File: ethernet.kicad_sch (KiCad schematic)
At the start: 32 parts, among them J8 RJ45_Wuerth_74980111211, U3 KSZ8001L-TR, U4 SRV05-4

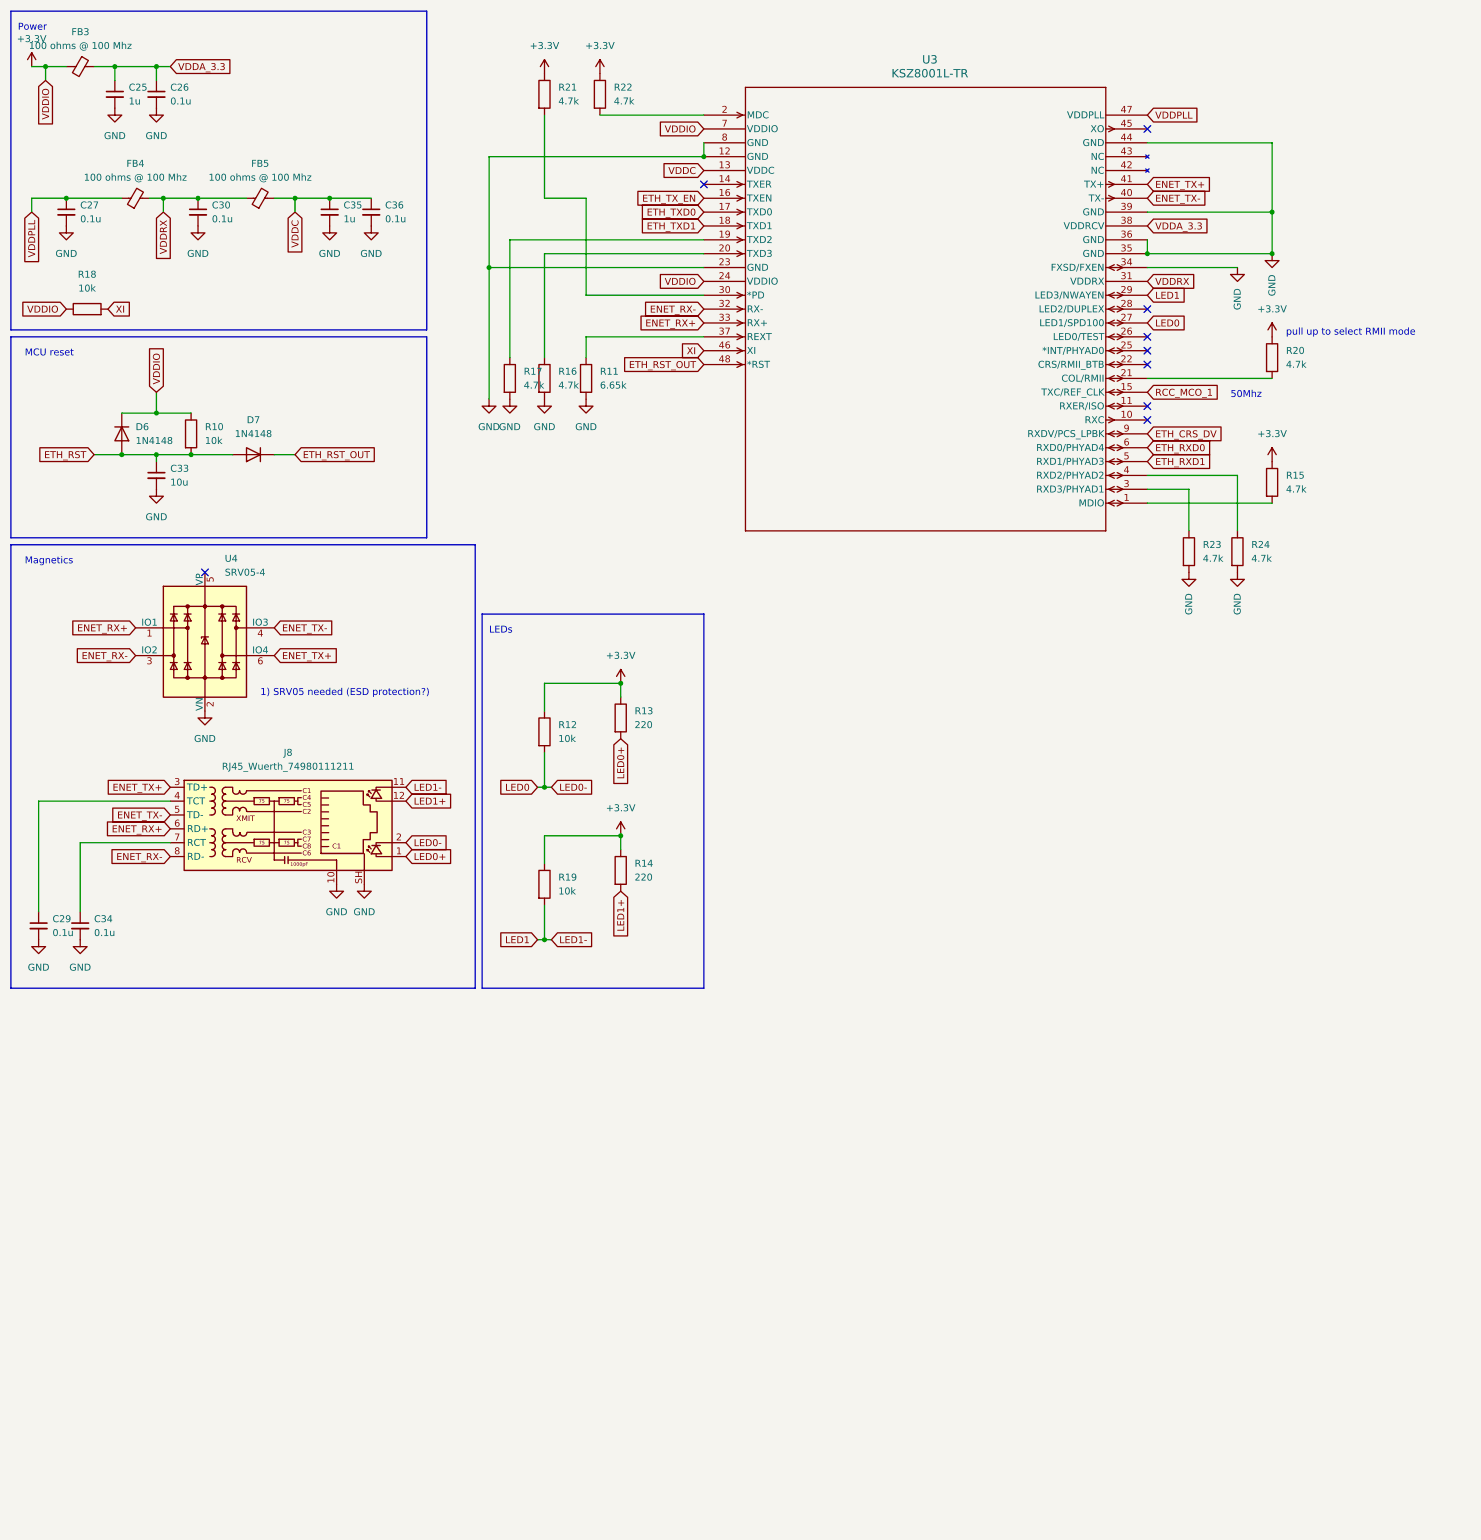
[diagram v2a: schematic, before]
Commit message: Switch over to using LAN8720A
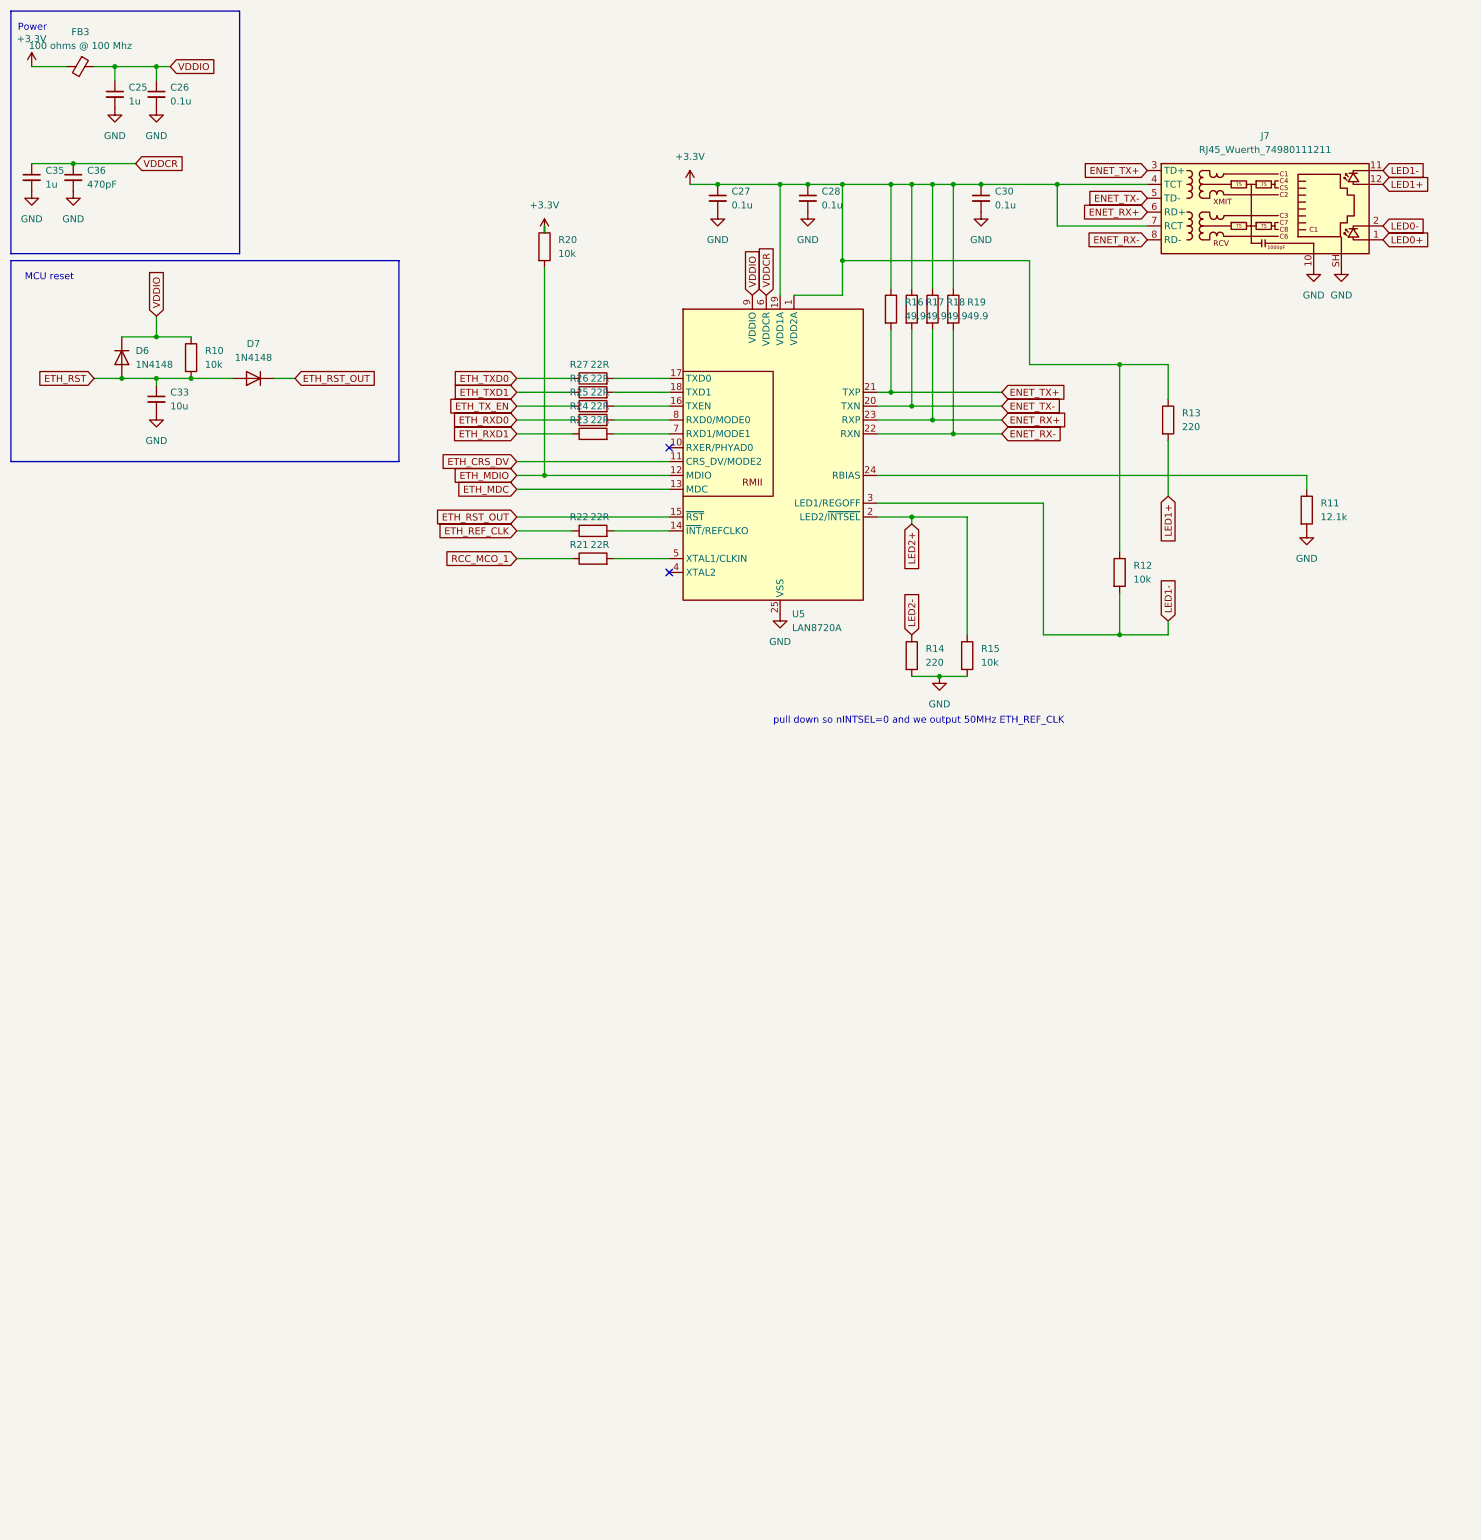
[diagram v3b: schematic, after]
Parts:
- removed C29, C34: 0.1u, symbol Device:C_Small
- removed FB4, FB5: 100 ohms @ 100 Mhz, symbol Device:FerriteBead_Small
- removed J8: RJ45_Wuerth_74980111211, Connector_RJ:RJ45_Wuerth_74980111211_Horizontal, symbol Connector:RJ45_Wuerth_74980111211
- removed U3: KSZ8001L-TR, LQFP-48_MCH, symbol 2024-02-18_02-27-55:KSZ8001L-TR
- removed U4: SRV05-4, Package_TO_SOT_SMD:SOT-23-6, symbol Power_Protection:SRV05-4
- added C28: 0.1u, symbol Device:C_Small
- added J7: RJ45_Wuerth_74980111211, Connector_RJ:RJ45_Wuerth_74980111211_Horizontal, symbol Connector:RJ45_Wuerth_74980111211
- added R25, R26, R27: 22R, symbol Device:R
- added U5: LAN8720A, Package_DFN_QFN:VQFN-24-1EP_4x4mm_P0.5mm_EP2.5x2.5mm_ThermalVias, symbol Interface_Ethernet:LAN8720A
- C36: value 0.1u -> 470pF
- R11: value 6.65k -> 12.1k
- R15, R20: value 4.7k -> 10k
- R16, R17: value 4.7k -> 49.9
- R18, R19: value 10k -> 49.9
- R21, R22, R23, R24: value 4.7k -> 22R
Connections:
- net LED1 is gone; now on net ENET_RX-: R19.2
- net VDDPLL is gone; now on net +3.3V: C27.1
- net VDDRX is gone; now on net +3.3V: C30.1
- net XI is gone; now on net ENET_RX+: R18.2
- net +3.3V: now also R16.1, R17.1, C28.1, J7.4 (TCT), J7.7 (RCT), U5.1 (VDD2A), U5.19 (VDD1A); no longer D6.1 (K), R10.1, R14.1, R15.1, R21.1, R22.1
- net ENET_RX+: now also J7.6 (RD+), U5.23 (RXP)
- net ENET_RX-: now also J7.8 (RD-), U5.22 (RXN)
- net ENET_TX+: now also R16.2, J7.3 (TD+), U5.21 (TXP)
- net ENET_TX-: now also R17.2, J7.5 (TD-), U5.20 (TXN)
- net ETH_CRS_DV: now also U5.11 (CRS_DV/MODE2)
- net ETH_RST_OUT: now also U5.15 (~{RST})
- net ETH_RXD0: now also R24.1
- net ETH_RXD1: now also R23.1
- net ETH_TXD0: now also R27.1
- net ETH_TXD1: now also R26.1
- net ETH_TX_EN: now also R25.1
- net GND: now also R14.2, R15.2, C28.2, J7.10, J7.SH, U5.25 (VSS); no longer R16.2, R17.2, R23.2, R24.2
- net LED0+: now also J7.1; no longer R13.2
- net LED1+: now also R13.2, J7.12; no longer R14.2
- net RCC_MCO_1: now also R21.1
- net at R11.1: now also U5.24 (RBIAS)
- net at R22.2: now also U5.14 (~{INT}/REFCLKO)
- net at R21.2: now also U5.5 (XTAL1/CLKIN)
- net ETH_MDIO: now reaches R20.2
- net ETH_MDIO: now also U5.12 (MDIO)
- net LED0 renamed LED1-
- net LED1-: now also J7.11, U5.3 (LED1/REGOFF)
- net VDDA_3.3 renamed VDDIO
- net VDDIO: now also D6.1 (K), R10.1, U5.9 (VDDIO)
- net VDDC renamed VDDCR
- net VDDCR: now also U5.6 (VDDCR)
- new net: R24.2, U5.8 (RXD0/MODE0)
- new net: R26.2, U5.18 (TXD1)
- new net: R27.2, U5.17 (TXD0)
- new net: R25.2, U5.16 (TXEN)
- new net: R23.2, U5.7 (RXD1/MODE1)
- new net ETH_MDC: U5.13 (MDC)
- new net ETH_REF_CLK: R22.1
- new net LED0-: J7.2
- new net LED2+: R15.1, U5.2 (LED2/~{INTSEL})
- new net LED2-: R14.1
- no-connect marks 9 -> 2
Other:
- note added: "pull down so nINTSEL=0 and we output 50MHz ETH_REF_CLK"
- note removed: "1) SRV05 needed (ESD protection?)"
- note removed: "50Mhz"
- note removed: "LEDs"
- note removed: "Magnetics"
- note removed: "pull up to select RMII mode"
- moved on the sheet: C33, C35, C36, D6, D7, R10, R12, R13

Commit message: Add USB circuit (peripheral mode only)
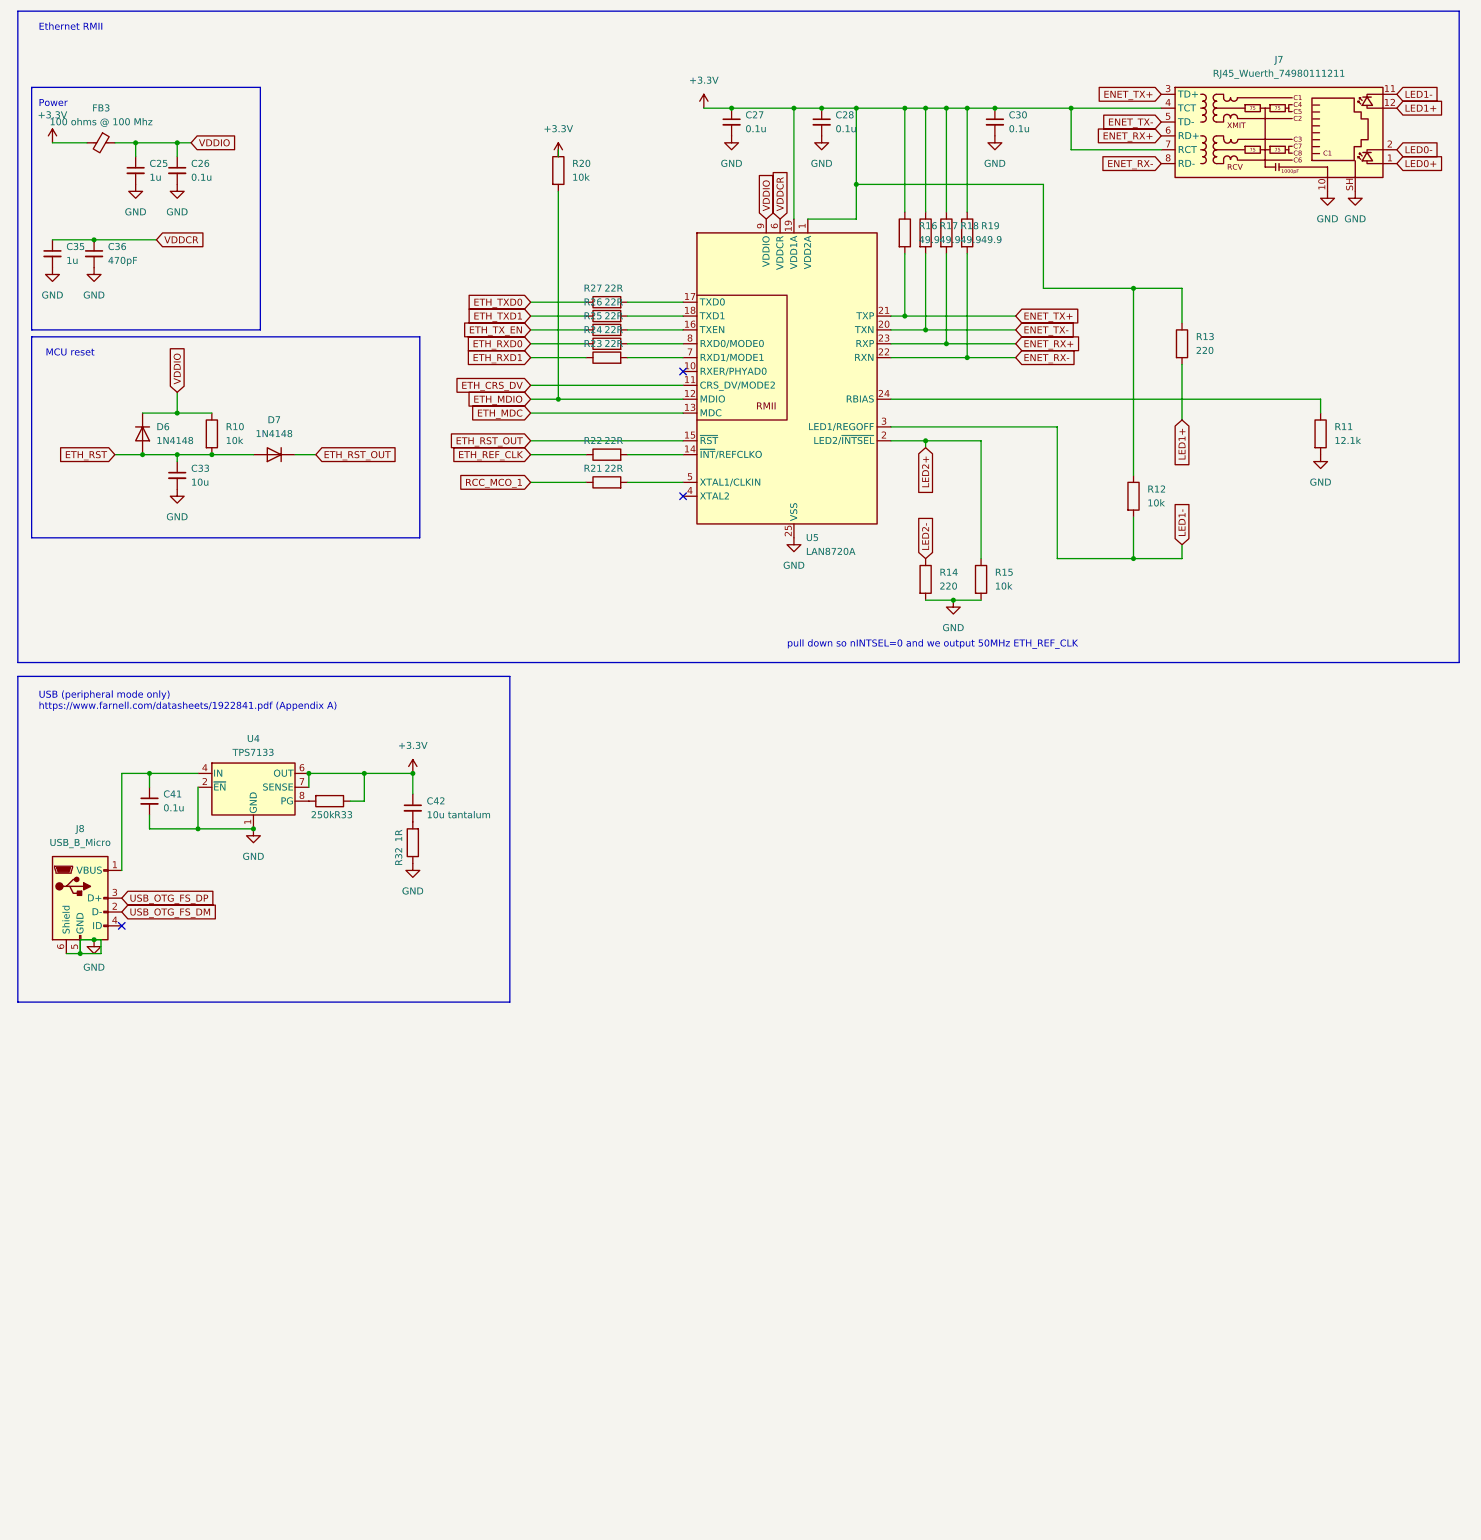
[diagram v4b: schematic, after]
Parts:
- added C41: 0.1u, symbol Device:C_Small
- added C42: 10u tantalum, symbol Device:C_Small
- added J8: USB_B_Micro, symbol Connector:USB_B_Micro
- added R32: 1R, symbol Device:R
- added R33: 250k, symbol Device:R
- added U4: TPS7133, symbol Regulator_Linear:TPS7133
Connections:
- net +3.3V: now also C42.1, R33.1, U4.5 (OUT), U4.6 (OUT), U4.7 (SENSE)
- net GND: now also C41.2, J8.5 (GND), J8.6 (Shield), R32.1, U4.1 (GND), U4.2 (~{EN})
- new net: C42.2, R32.2
- new net: C41.1, J8.1 (VBUS), U4.3 (IN), U4.4 (IN)
- new net: R33.2, U4.8 (PG)
- new net USB_OTG_FS_DM: J8.2 (D-)
- new net USB_OTG_FS_DP: J8.3 (D+)
- no-connect marks 2 -> 3
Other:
- note added: "Ethernet RMII"
- note added: "USB (peripheral mode only) https://www.farnell.com/datasheets/1922841.pdf (Appendix A)"
- moved on the sheet: C25, C26, C27, C28, C30, C33, C35, C36, D6, D7, FB3, J7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
